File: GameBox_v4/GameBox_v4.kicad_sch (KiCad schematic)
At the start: 22 parts, among them J1 OLED, J2 Conn_01x08, SW1 ON/OFF, SW2 SW_up, SW3 SW_down, SW4 SW_right, SW5 SW_left, SW6 SW_select, U1 ATmega328P-A, U2 3.3V_boost_regulator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

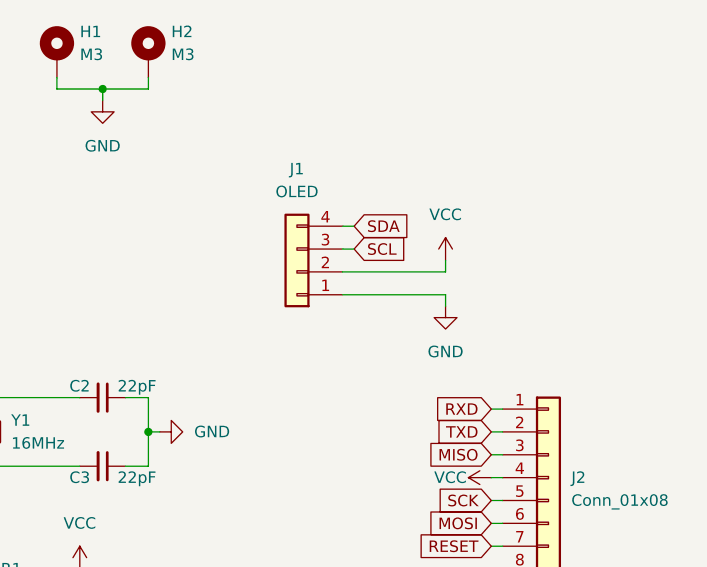
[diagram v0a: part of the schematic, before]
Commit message: fixed OLEDs
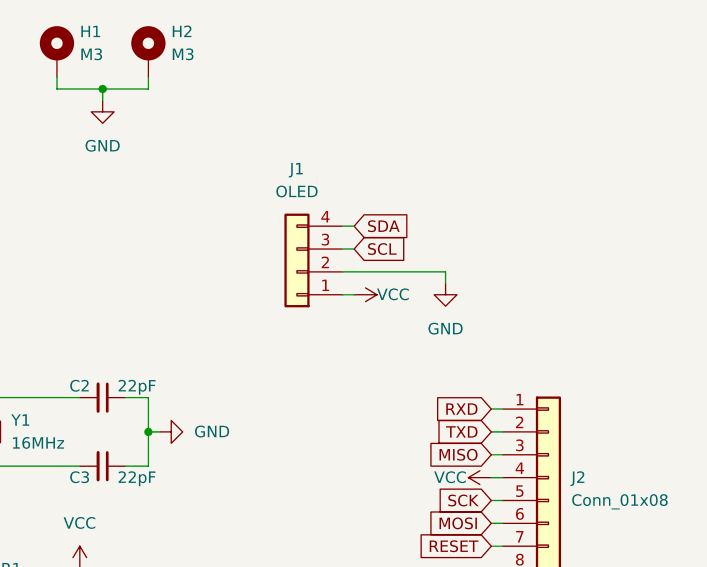
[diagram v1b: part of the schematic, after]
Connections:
- net GND: now also J1.2 (Pin_2); no longer J1.1 (Pin_1)
- net VCC: now also J1.1 (Pin_1); no longer J1.2 (Pin_2)
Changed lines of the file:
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@@
+    (stroke (width 0) (type default) (color 0 0 0 0))
+  )
+  (wire (pts (xy 198.12 87.63) (xy 199.39 87.63))
     (stroke (width 0) (type default) (color 0 0 0 0))
   )
@@
     (stroke (width 0) (type default) (color 0 0 0 0))
   )
-  (wire (pts (xy 198.12 87.63) (xy 209.55 87.63))
+  (wire (pts (xy 198.12 85.09) (xy 209.55 85.09))
     (stroke (width 0) (type default) (color 0 0 0 0))
   )
@@
     (stroke (width 0) (type default) (color 0 0 0 0))
   )
-  (wire (pts (xy 209.55 87.63) (xy 209.55 88.9))
+  (wire (pts (xy 209.55 85.09) (xy 209.55 86.36))
     (stroke (width 0) (type default) (color 0 0 0 0))
   )
@@
     (stroke (width 0) (type default) (color 0 0 0 0))
   )
-  (wire (pts (xy 198.12 85.09) (xy 209.55 85.09))
-    (stroke (width 0) (type default) (color 0 0 0 0))
-  )
   (wire (pts (xy 140.97 139.7) (xy 180.34 139.7))
     (stroke (width 0) (type default) (color 0 0 0 0))
@@
   )
   (wire (pts (xy 171.45 64.77) (xy 166.37 64.77))
-    (stroke (width 0) (type default) (color 0 0 0 0))
-  )
-  (wire (pts (xy 209.55 85.09) (xy 209.55 83.82))
     (stroke (width 0) (type default) (color 0 0 0 0))
   )
@@
     )
   )
-  (symbol (lib_id "power:VCC") (at 209.55 83.82 0) (unit 1)
-    (in_bom yes) (on_board yes) (fields_autoplaced)
-    (property "Reference" "#PWR06" (id 0) (at 209.55 87.63 0)
-      (effects (font (size 1.27 1.27)) hide)
-    )
-    (property "Value" "VCC" (id 1) (at 209.55 78.74 0))
-    (property "Footprint" "" (id 2) (at 209.55 83.82 0)
-      (effects (font (size 1.27 1.27)) hide)
-    )
-    (property "Datasheet" "" (id 3) (at 209.55 83.82 0)
+  (symbol (lib_id "power:VCC") (at 199.39 87.63 270) (unit 1)
+    (in_bom yes) (on_board yes)
+    (property "Reference" "#PWR06" (id 0) (at 195.58 87.63 0)
+      (effects (font (size 1.27 1.27)) hide)
+    )
+    (property "Value" "VCC" (id 1) (at 201.93 87.63 90)
+      (effects (font (size 1.27 1.27)) (justify left))
+    )
+    (property "Footprint" "" (id 2) (at 199.39 87.63 0)
+      (effects (font (size 1.27 1.27)) hide)
+    )
+    (property "Datasheet" "" (id 3) (at 199.39 87.63 0)
       (effects (font (size 1.27 1.27)) hide)
     )
@@
     (pin "2")
   )
-  (symbol (lib_id "power:GND") (at 209.55 88.9 0) (unit 1)
-    (in_bom yes) (on_board yes) (fields_autoplaced)
-    (property "Reference" "#PWR07" (id 0) (at 209.55 95.25 0)
-      (effects (font (size 1.27 1.27)) hide)
-    )
-    (property "Value" "GND" (id 1) (at 209.55 93.98 0))
-    (property "Footprint" "" (id 2) (at 209.55 88.9 0)
-      (effects (font (size 1.27 1.27)) hide)
-    )
-    (property "Datasheet" "" (id 3) (at 209.55 88.9 0)
-      (effects (font (size 1.27 1.27)) hide)
-    )
+  (symbol (lib_id "power:GND") (at 209.55 86.36 0) (unit 1)
+    (in_bom yes) (on_board yes) (fields_autoplaced)
+    (property "Reference" "#PWR07" (id 0) (at 209.55 92.71 0)
+      (effects (font (size 1.27 1.27)) hide)
+    )
+    (property "Value" "GND" (id 1) (at 209.55 91.44 0))
+    (property "Footprint" "" (id 2) (at 209.55 86.36 0)
+      (effects (font (size 1.27 1.27)) hide)
+    )
+    (property "Datasheet" "" (id 3) (at 209.55 86.36 0)
+      (effects (font (size 1.27 1.27)) hide)
+    )
